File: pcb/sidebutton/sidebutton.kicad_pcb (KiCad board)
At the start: 2 copper layers, 32 x 19.5 mm, 7 parts, among them J1 Conn_01x04, SW1 SW_DIP_x01

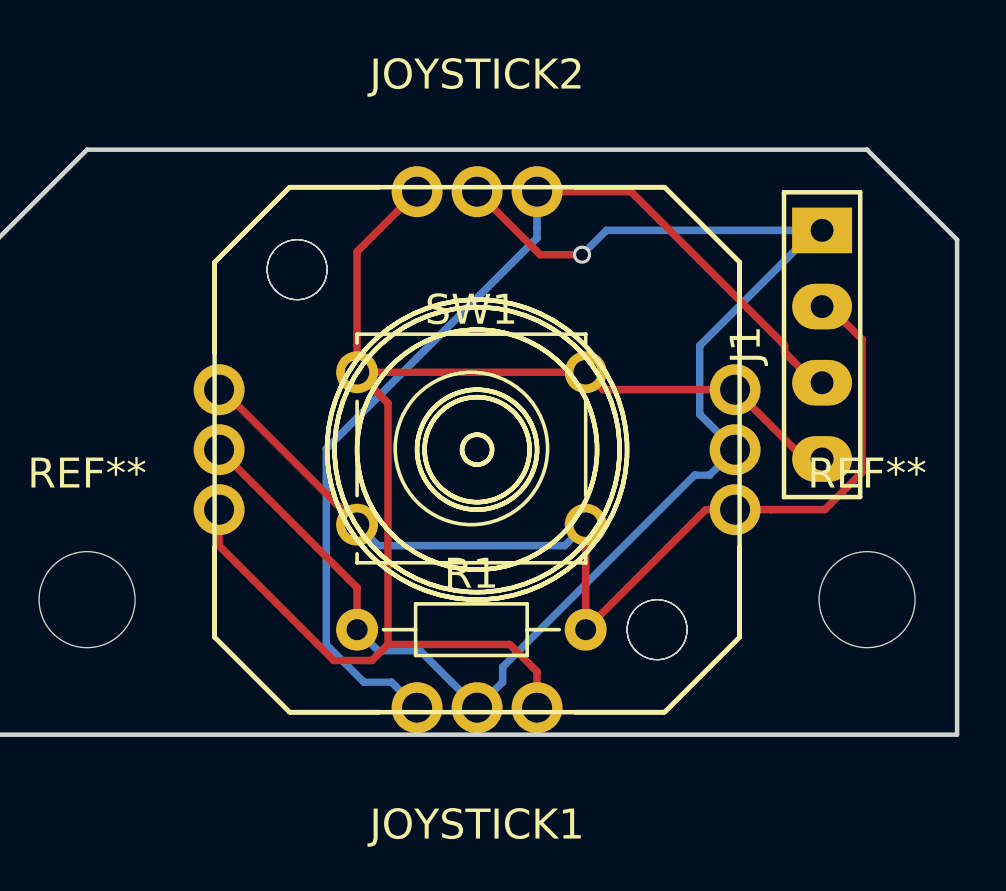
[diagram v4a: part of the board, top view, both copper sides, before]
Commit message: sidebutton use KH key
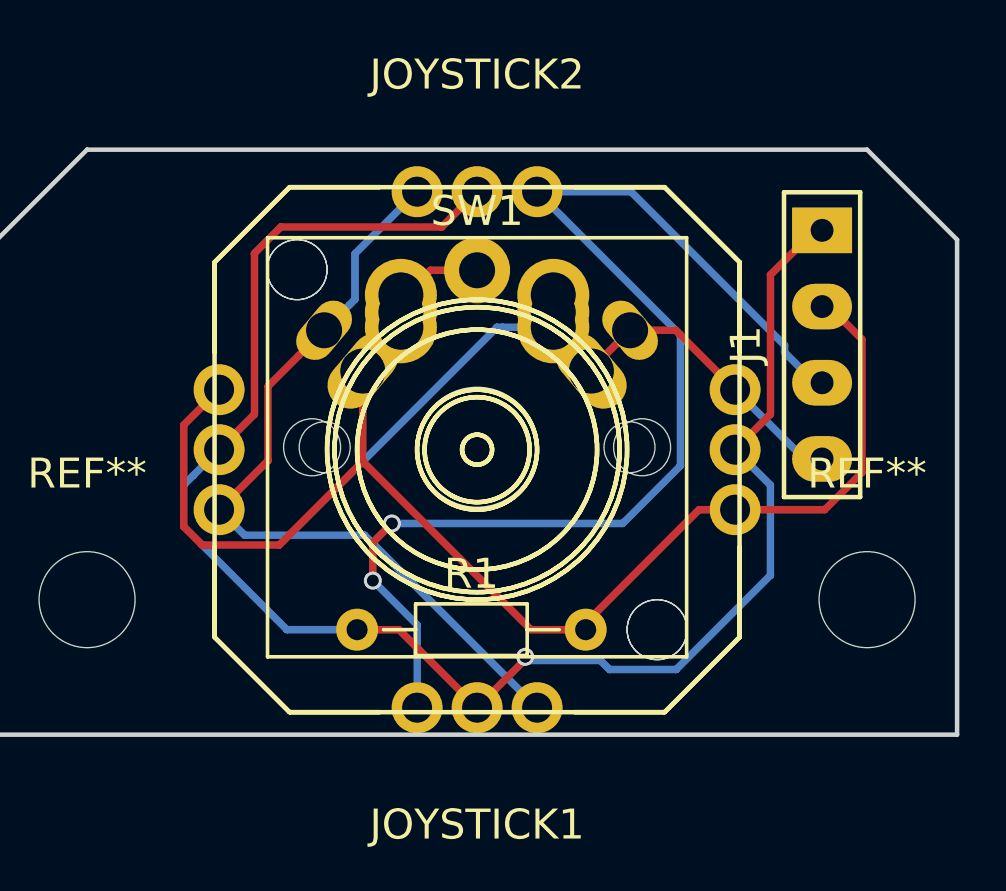
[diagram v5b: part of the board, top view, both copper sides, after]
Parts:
- SW1: footprint Buttons_Switches_THT:SW_Tactile_Straight_KSA0Axx1LFTR -> 4x6t2:MX_ALPS_KH_u1.00
- moved SW1 4.72 mm to (13.0, -5.08)
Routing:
- net /out1: track 35.8 -> 47.8 mm
- net +5V: track 47.8 -> 56.0 mm
- net /out2: track 34.2 -> 40.8 mm, vias 0 -> 2
- net GND: track 48.2 -> 50.4 mm
